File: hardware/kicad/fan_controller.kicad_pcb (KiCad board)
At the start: 2 copper layers, 75 x 60 mm, 78 parts, among them J1 12V IN, J10 AIN2, J11 AIN3, J12 AIN4, J13 AIN5, J14 AIN6, J2 BluePill A, J3 BluePill B, J5 FAN1, J6 FAN2, J7 FAN3, J8 FAN4, J9 AIN1, Q1 BSS138, Q2 BSS138, Q3 BSS138, Q4 BSS138

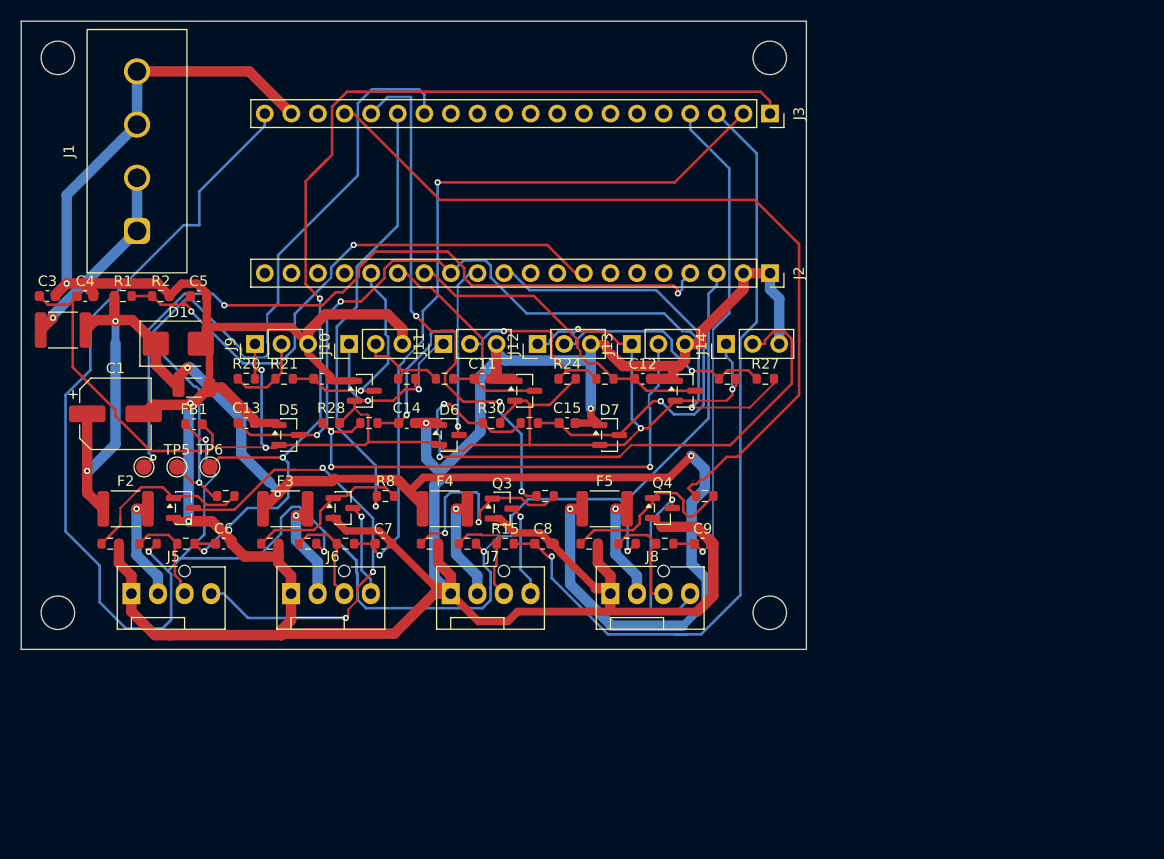
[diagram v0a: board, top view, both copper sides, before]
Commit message: hw: sync schematic to board after removing TP1/TP4 test points
Board no longer carries TP1 (+12V probe) and TP4 (NRST probe); remove
the matching symbols and their orphaned net labels from the schematic
so both files agree. Cross-checked all 77 references: footprints and
values now match exactly between schematic and board.

ERC: 0 errors, 4 warnings (pre-existing single-pin-label style,
consistent with the rest of the sheet).

Signed-off-by: Roman Skakun <rm.skakun@gmail.com>
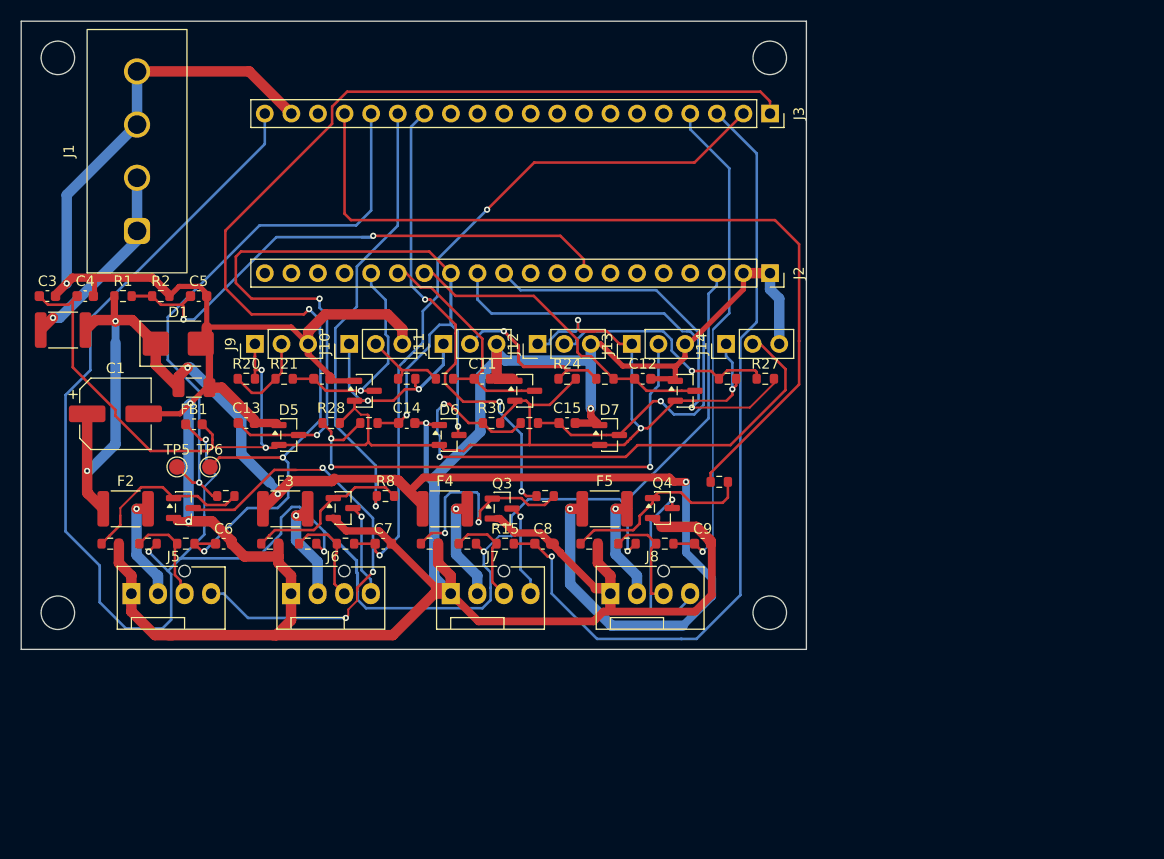
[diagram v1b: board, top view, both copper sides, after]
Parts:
- removed TP4: NRST, TestPoint:TestPoint_Pad_D1.5mm
- moved R16 1.93 mm to (66.7, 44.0)
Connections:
- J2 pad 12: AIN5 -> AIN4
- J2 pad 13: AIN4 -> AIN5
- J3 pad 14: FAN1_PWM -> FAN3_PWM
- J3 pad 16: FAN3_PWM -> FAN1_PWM
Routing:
- net NRST: track 73.5 -> 0.00 mm, vias 3 -> 0
- net FAN1_PWM: track 72.8 -> 54.9 mm
- net AIN4: track 78.8 -> 96.4 mm
- net AIN5: track 31.2 -> 39.9 mm
- net FAN1_TACH: track 107.6 -> 115.6 mm
- net FAN3_PWM: track 52.5 -> 46.1 mm
- net FAN2_TACH: track 73.1 -> 68.9 mm
- net +12V: track 144.6 -> 140.5 mm
- net AIN6_IN: track 59.7 -> 56.0 mm
- net +3V3A: track 160.1 -> 163.7 mm
- net V12_SENSE: track 55.4 -> 52.6 mm
- net FAN4_PWM: track 78.4 -> 80.5 mm
- net GND: track 356.5 -> 357.8 mm
- net FAN4_PWM_G: track 17.8 -> 18.9 mm
- net +3V3: track 188.1 -> 187.3 mm
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
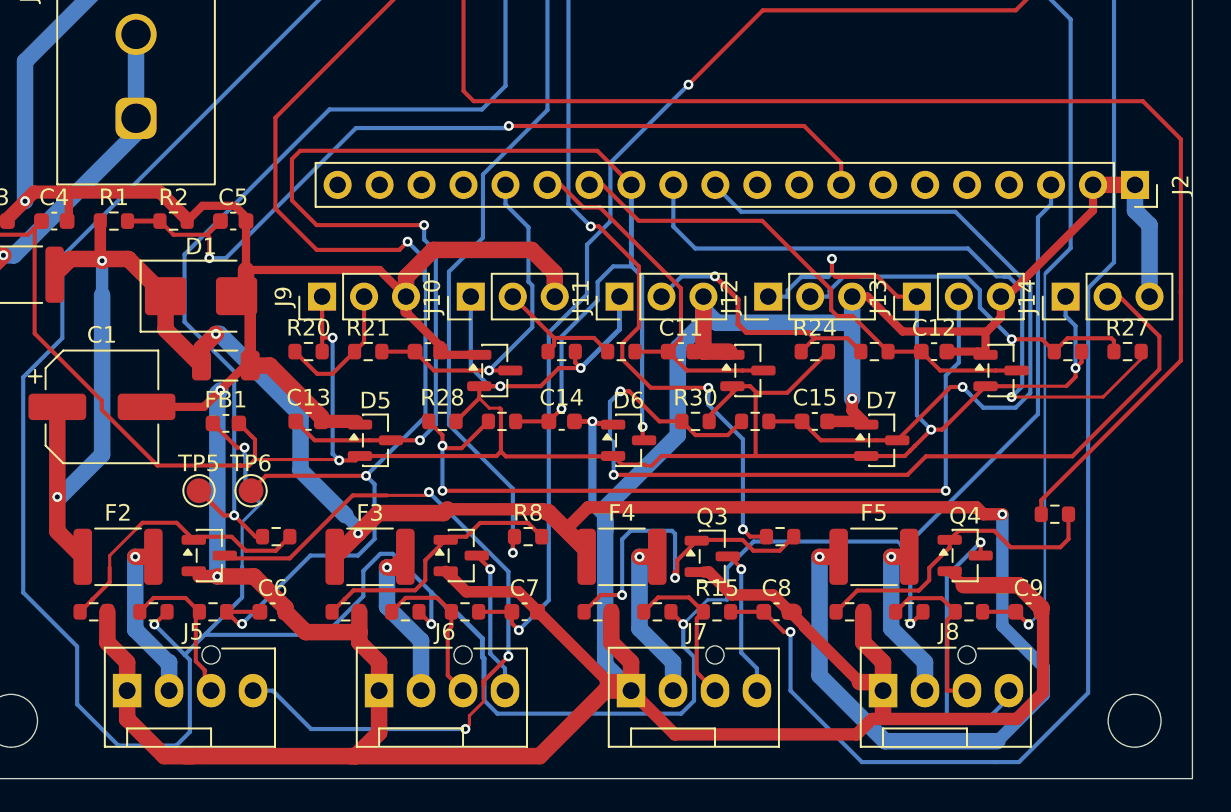
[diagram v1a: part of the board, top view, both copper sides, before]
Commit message: hw: sync schematic to board after removing TP5/TP6, regen render
Board no longer carries TP5 (FAN1_PWM probe) and TP6 (FAN1_TACH
probe); remove the matching symbols and their orphaned net labels
from the schematic so both files agree. Cross-checked all 75
references: footprints match exactly between schematic and board.

ERC: 0 errors, 4 warnings (pre-existing single-pin-label style).
Regenerated hardware/pcb_3d.png at current board state.

Signed-off-by: Roman Skakun <rm.skakun@gmail.com>
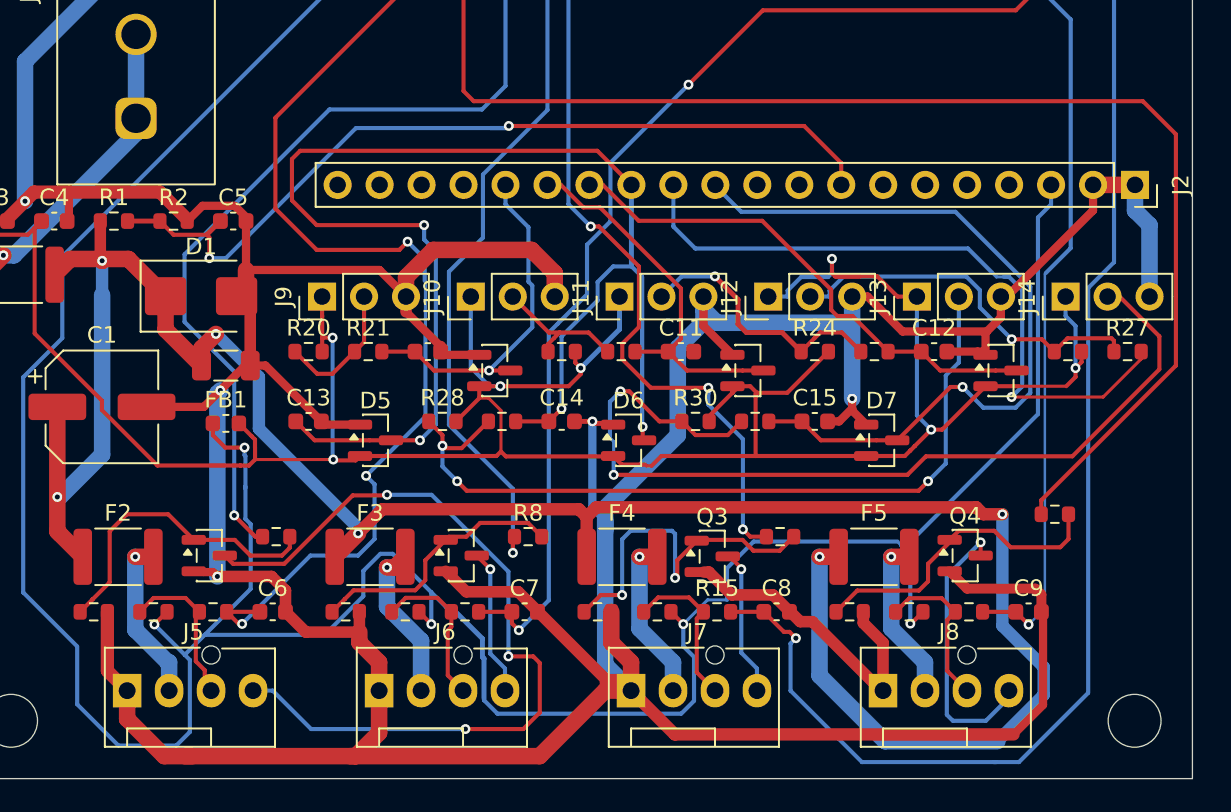
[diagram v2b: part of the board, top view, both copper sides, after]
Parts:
- removed TP5: FAN1_PWM, TestPoint:TestPoint_Pad_D1.5mm
- removed TP6: FAN1_TACH, TestPoint:TestPoint_Pad_D1.5mm
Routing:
- net FAN1_TACH: track 115.6 -> 108.3 mm
- net FAN1_PWM_OUT: track 45.3 -> 50.0 mm
- net FAN1_PWM: track 54.9 -> 52.2 mm
- net AIN5_IN: track 50.6 -> 48.8 mm
- net FAN1_PWM_G: track 17.1 -> 18.8 mm
- net FAN4_TACH_IN: track 10.5 -> 9.76 mm
- net GND: track 357.8 -> 357.2 mm

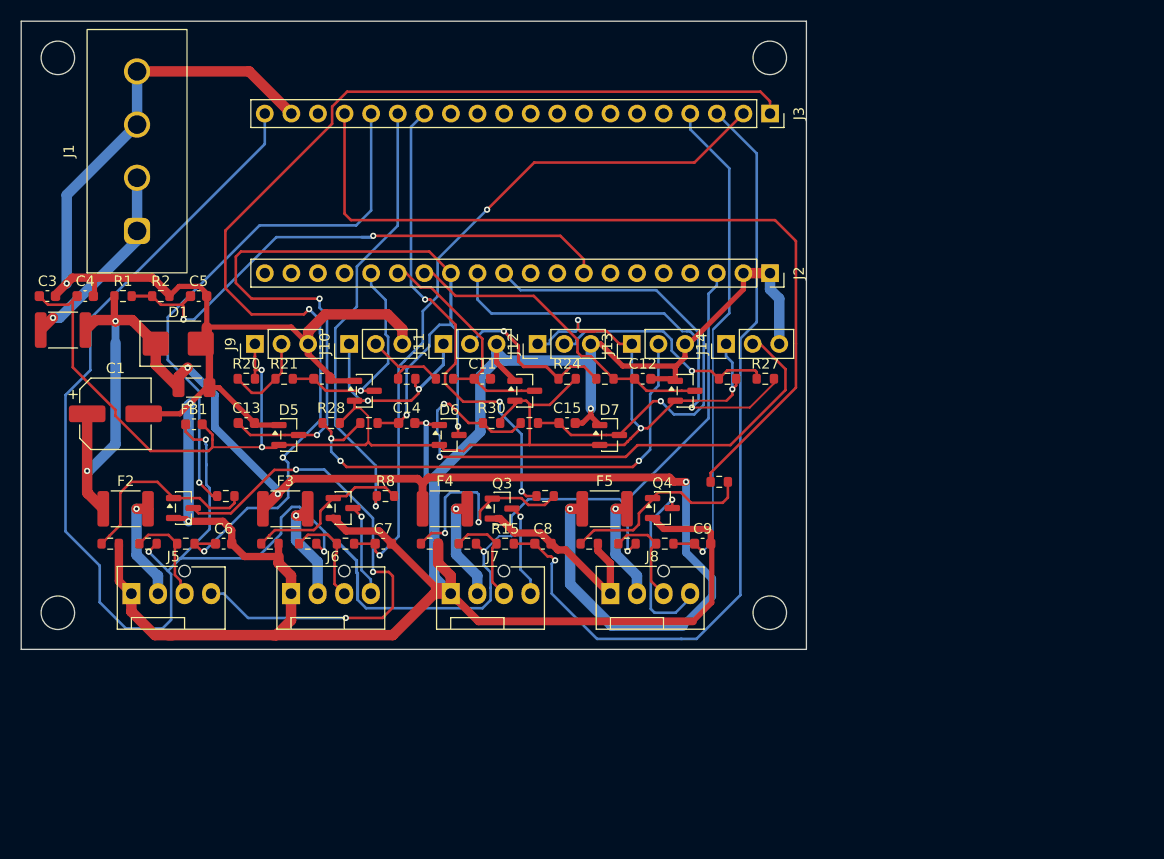
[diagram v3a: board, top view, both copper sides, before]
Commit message: hw: fix AIN4/AIN5 short and split GND net on PCB
Resolve every DRC error on fan_controller.kicad_pcb. Only the 14
silk_overlap warnings remain, and those are cosmetic.

AIN4 was routed to the wrong Blue Pill pin. Its F.Cu track ended on
J2 pad 13 (AIN5) at (41.045, 24.065) instead of pad 12 (AIN4) at
(43.585, 24.065), one 2.54 mm pitch away. That shorted the two analog
inputs and left pad 12's own B.Cu stub orphaned, which showed up as a
shorting_items error, a solder_mask_bridge error and an
unconnected_items error. The short is present in the committed gerbers,
so the boards described by hardware/gerbers read the same voltage on
AIN4 and AIN5. Replace the bad diagonal with a horizontal run to
(41.52, 22.0) and a 45 degree diagonal into pad 12.

GND was split into three islands rather than one. The second island
held the whole FAN3 ground branch (J8.1, Q3.2, R17.2, C8.2), so that
fan header had no ground return at all and its BSS138 could not pull
the PWM line low. Join it to the main GND bus with a 1 mm F.Cu link
from J8.1 down to the y=57.325 bus. The third island was C11.2 alone,
the 100 nF analog decoupling cap; connect it with a 0.5 mm F.Cu run
east to the existing GND diagonal.

Also drop four leftovers that carried no pad: a 0.05 mm AIN5 stub, a
1.46 mm +3V3A stub already covered by a longer parallel run, a 1.0 mm
V12_SENSE stub and a single-layer FAN1_TACH via.

Per-net island counts are unchanged except AIN4 (2 -> 1) and GND
(3 -> 1), so no other connection moved. The gerbers under
hardware/gerbers predate these fixes and still need re-exporting.

Signed-off-by: Roman Skakun <rm.skakun@gmail.com>
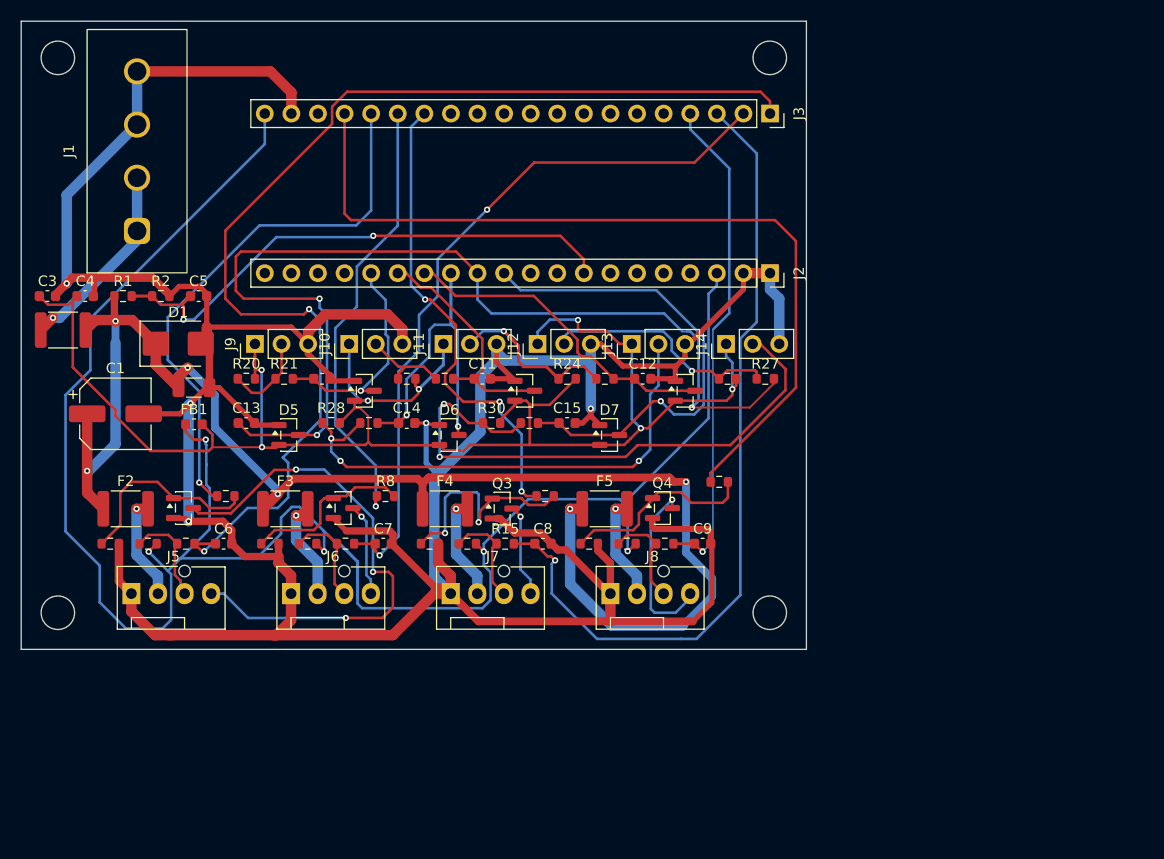
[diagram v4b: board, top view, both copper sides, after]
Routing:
- net GND: track 357.2 -> 364.3 mm
- net AIN4: track 96.4 -> 99.3 mm
- net +3V3A: track 163.6 -> 162.2 mm
- net V12_SENSE: track 52.6 -> 51.6 mm
- net FAN1_TACH: track 108.3 -> 108.9 mm, vias 3 -> 2
- net +3V3: track 187.3 -> 186.7 mm
- net FAN2_PWM_G: track 16.0 -> 16.5 mm
